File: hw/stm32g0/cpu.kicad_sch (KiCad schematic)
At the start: 42 parts, among them J201 Conn_01x06, J202 Conn_01x04, J203 Conn_01x05, U201 STM32G030K8Tx, U202 74AHCT125, U203 CAT24C256

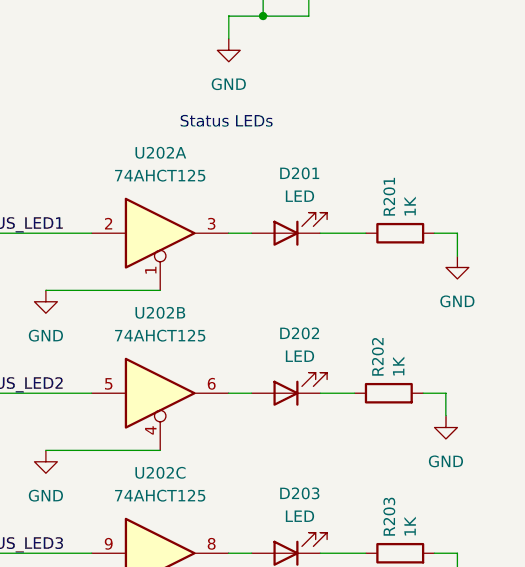
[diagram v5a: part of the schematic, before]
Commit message: fix(fw): fix red and yellow LEDs resistors
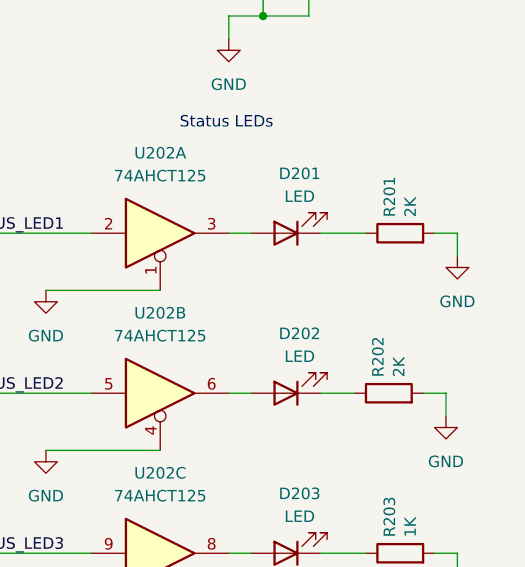
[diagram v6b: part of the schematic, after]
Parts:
- R201, R202: value 1K -> 2K
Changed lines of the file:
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@@
 			)
 		)
-		(property "Value" "1K"
+		(property "Value" "2K"
 			(at 270.383 93.472 0)
 			(effects
@@
 			)
 		)
-		(property "Value" "1K"
+		(property "Value" "2K"
 			(at 271.653 75.692 0)
 			(effects

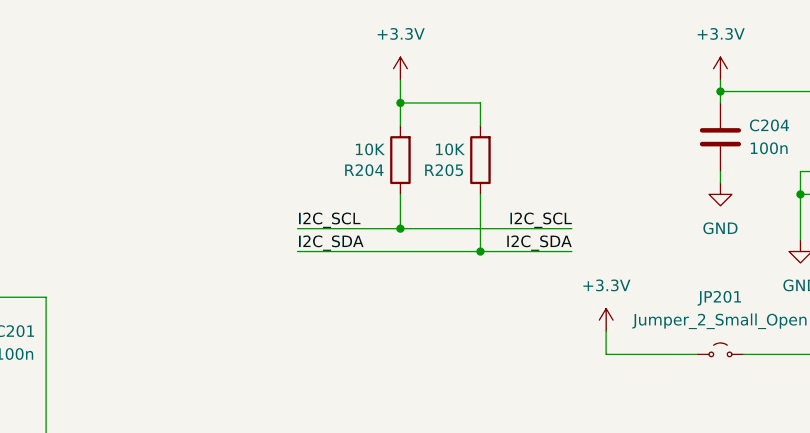
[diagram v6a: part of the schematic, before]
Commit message: fix(hw): make I2C pull-up stronger
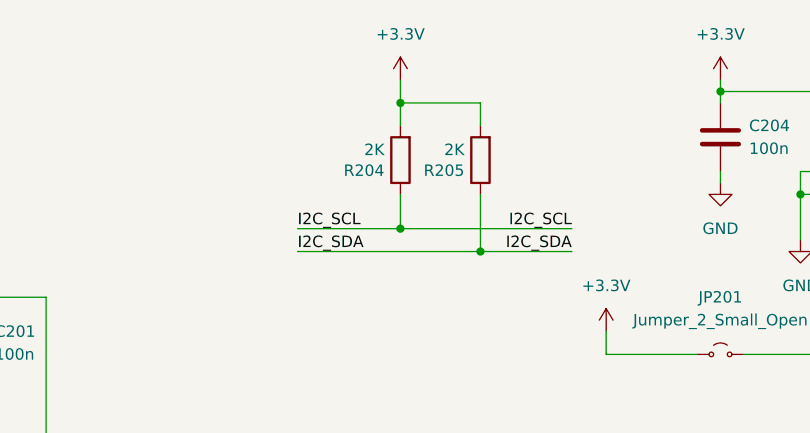
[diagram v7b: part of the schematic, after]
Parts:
- R204, R205: value 10K -> 2K
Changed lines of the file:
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@@
 			)
 		)
-		(property "Value" "10K"
+		(property "Value" "2K"
 			(at 131.572 31.877 0)
 			(effects
@@
 			)
 		)
-		(property "Value" "10K"
+		(property "Value" "2K"
 			(at 122.682 31.877 0)
 			(effects
